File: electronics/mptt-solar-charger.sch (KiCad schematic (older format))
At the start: 46 parts

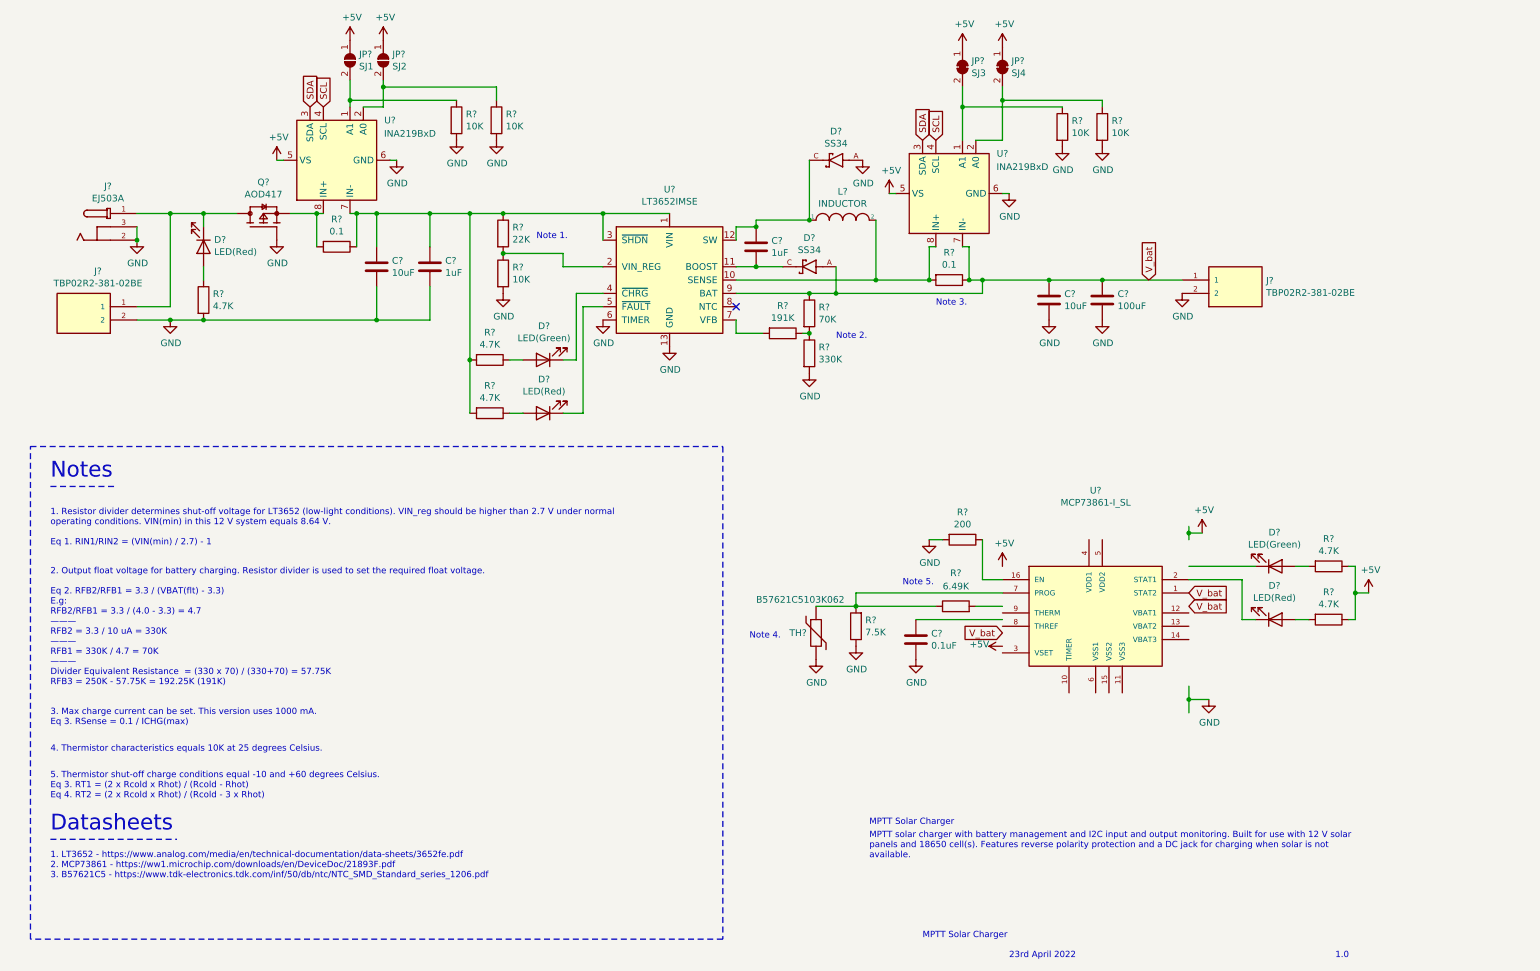
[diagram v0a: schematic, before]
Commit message: updated mcp73861 symbol
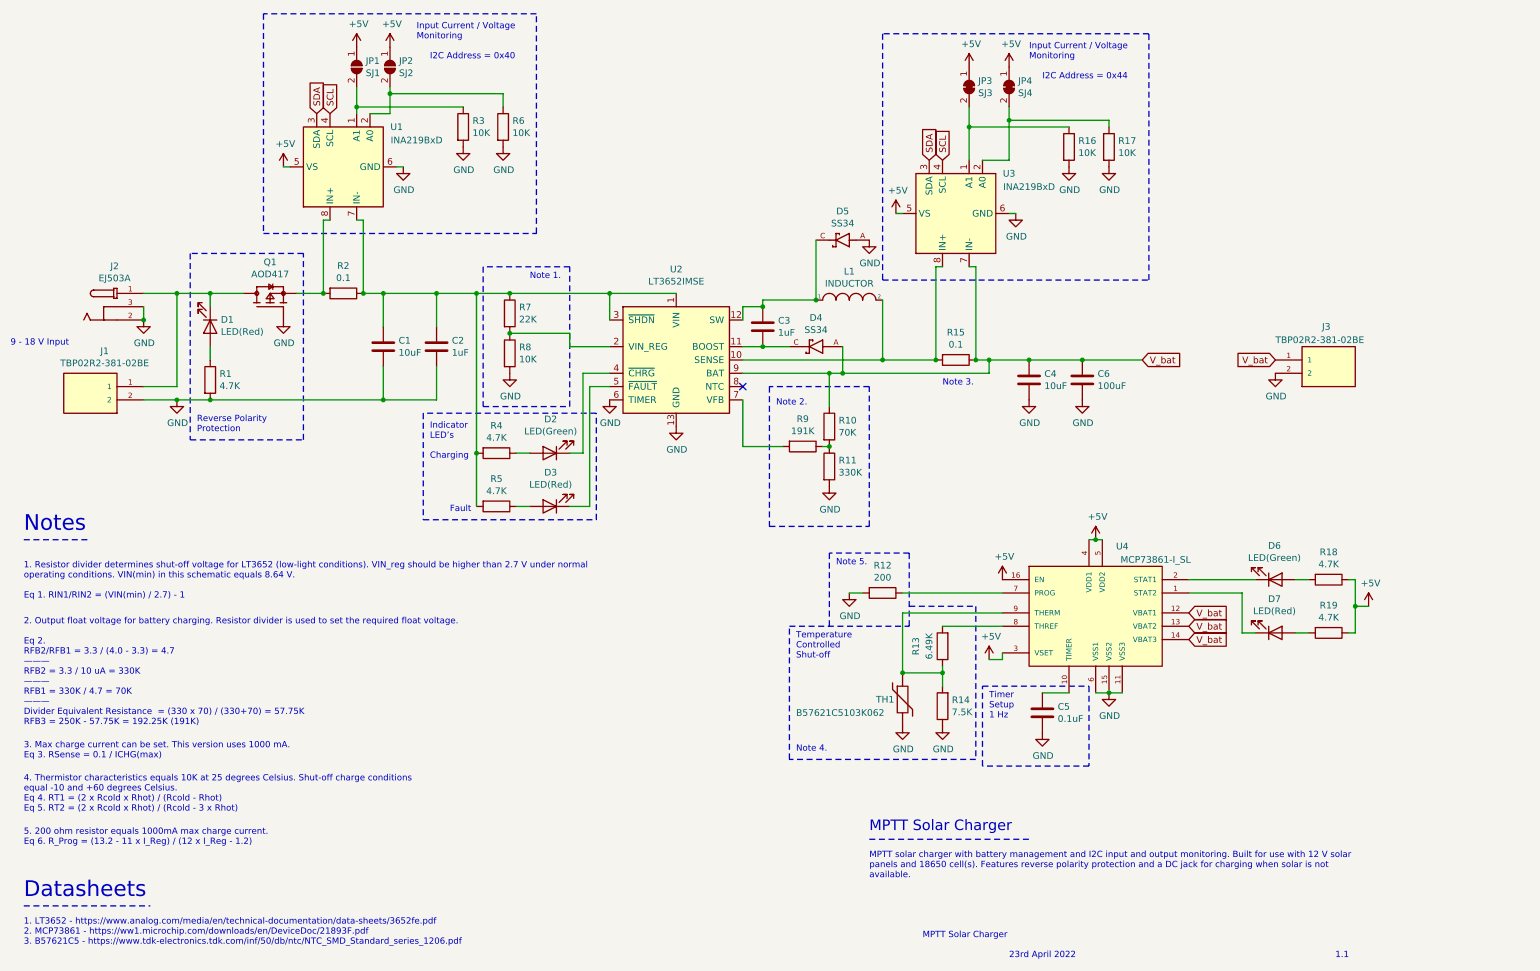
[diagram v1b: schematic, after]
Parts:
- gave numbers to parts that had none: 46
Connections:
- wire segments 113 -> 114
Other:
- note added: "1. Resistor divider determines shut-off voltage for LT3652 (low-light conditions). VIN_reg should be higher than 2.7 V under normal \noperating conditions. VIN(min) in this schematic equals 8.64 V.\n\nEq 1. RIN1/RIN2 = (VIN(min) / 2.7) - 1"
- note added: "1.1"
- note added: "2. Output float voltage for battery charging. Resistor divider is used to set the required float voltage. \n\nEq 2. \nRFB2/RFB1 = 3.3 / (4.0 - 3.3) = 4.7\n———\nRFB2 = 3.3 / 10 uA = 330K\n———\nRFB1 = 330K / 4.7 = 70K\n———\nDivider Equivalent Resistance = (330 x 70) / (330+70) = 57.75K\nRFB3 = 250K - 57.75K = 192.25K (191K)"
- note added: "4. Thermistor characteristics equals 10K at 25 degrees Celsius. Shut-off charge conditions \nequal -10 and +60 degrees Celsius. \nEq 4. RT1 = (2 x Rcold x Rhot) / (Rcold - Rhot)\nEq 5. RT2 = (2 x Rcold x Rhot) / (Rcold - 3 x Rhot)"
- note added: "5. 200 ohm resistor equals 1000mA max charge current.\nEq 6. R_Prog = (13.2 - 11 x I_Reg) / (12 x I_Reg - 1.2)"
- note added: "9 - 18 V Input"
- note added: "Charging"
- note added: "Fault"
- note added: "I2C Address = 0x40"
- note added: "I2C Address = 0x44"
- note added: "Indicator\nLED’s"
- note added: "Input Current / Voltage\nMonitoring"
- note added: "Reverse Polarity \nProtection"
- note added: "Temperature \nControlled \nShut-off"
- note added: "Timer\nSetup\n1 Hz"
- note removed: "1. Resistor divider determines shut-off voltage for LT3652 (low-light conditions). VIN_reg should be higher than 2.7 V under normal \noperating conditions. VIN(min) in this 12 V system equals 8.64 V.\n\nEq 1. RIN1/RIN2 = (VIN(min) / 2.7) - 1"
- note removed: "1.0"
- note removed: "2. Output float voltage for battery charging. Resistor divider is used to set the required float voltage. \n\nEq 2. RFB2/RFB1 = 3.3 / (VBAT(flt) - 3.3)\nE.g: \nRFB2/RFB1 = 3.3 / (4.0 - 3.3) = 4.7\n———\nRFB2 = 3.3 / 10 uA = 330K\n———\nRFB1 = 330K / 4.7 = 70K\n———\nDivider Equivalent Resistance = (330 x 70) / (330+70) = 57.75K\nRFB3 = 250K - 57.75K = 192.25K (191K)"
- note removed: "4. Thermistor characteristics equals 10K at 25 degrees Celsius."
- note removed: "5. Thermistor shut-off charge conditions equal -10 and +60 degrees Celsius. \nEq 3. RT1 = (2 x Rcold x Rhot) / (Rcold - Rhot)\nEq 4. RT2 = (2 x Rcold x Rhot) / (Rcold - 3 x Rhot)"
- moved on the sheet: C1, C2, C3, C4, C5, C6, D1, D2, D3, D4, D5, D6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

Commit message: removed unneeded bypass cap on LT3652 input
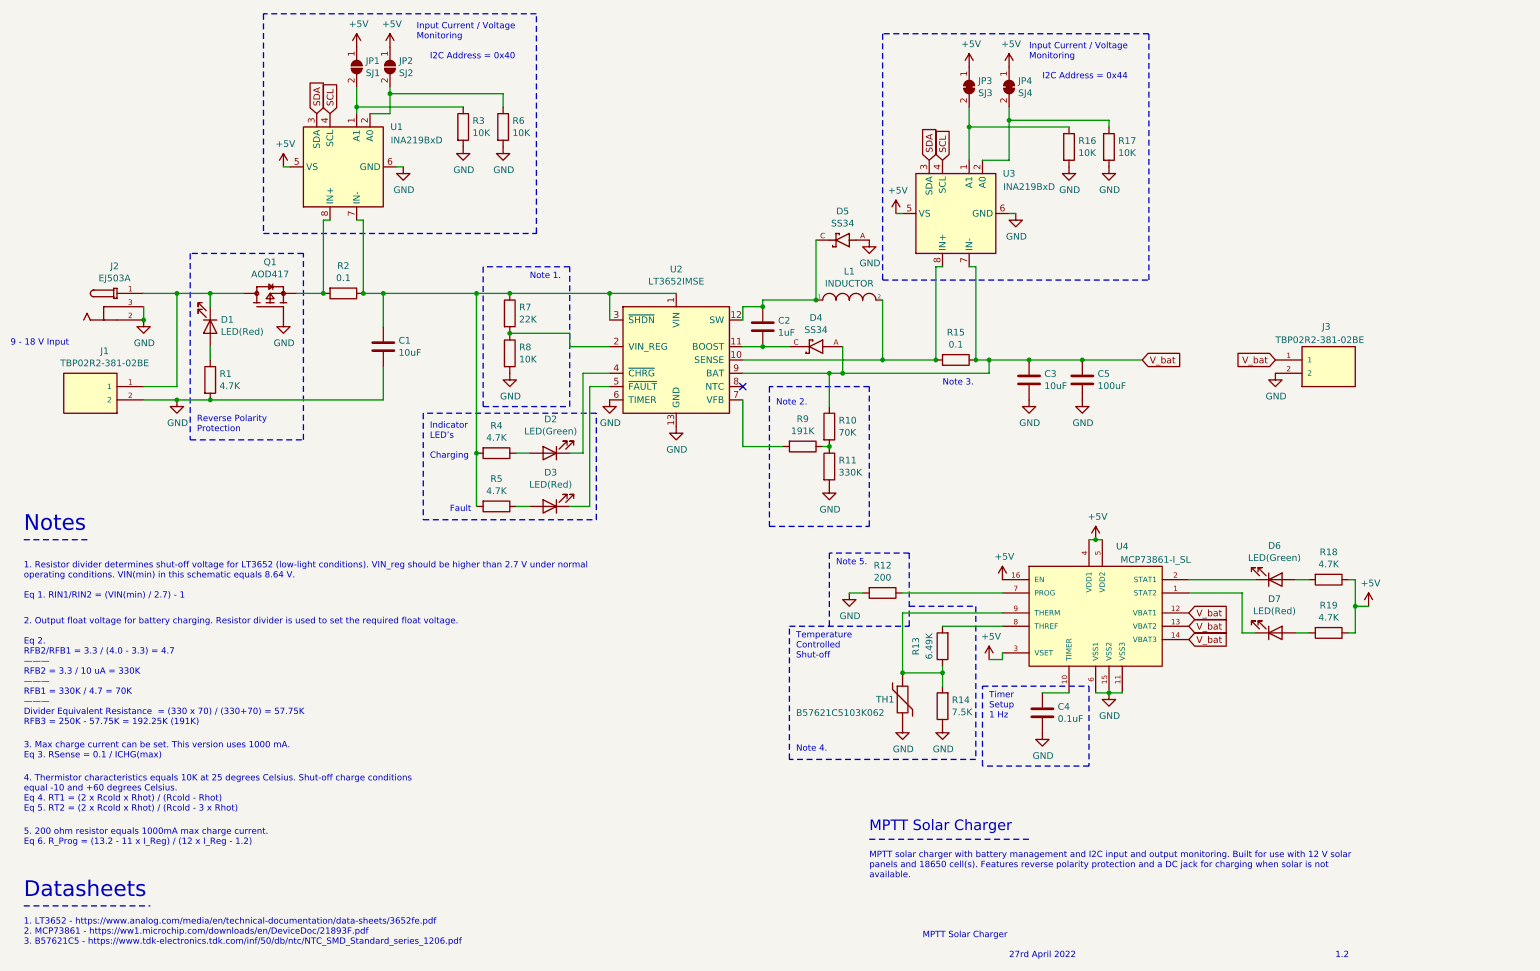
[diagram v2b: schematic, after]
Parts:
- removed C2: 1uF, symbol Device:C
- renumbered C3 to C2, C4 to C3, C5 to C4, C6 to C5
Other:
- note added: "1.2"
- note added: "27rd April 2022"
- note removed: "1.1"
- note removed: "23rd April 2022"
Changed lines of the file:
@@
 	3400 2650 3400 2900
 Connection ~ 2100 3450
-$Comp
-L Device:C C2
-U 1 1 6264ABCC
-P 3800 3050
-F 0 "C2" H 3915 3096 50  0000 L CNN
-F 1 "1uF" H 3915 3005 50  0000 L CNN
-F 2 "" H 3838 2900 50  0001 C CNN
-F 3 "~" H 3800 3050 50  0001 C CNN
-	1    3800 3050
-	1    0    0    -1
-$EndComp
-Wire Wire Line
-	3800 3450 3800 3200
-Wire Wire Line
-	3800 2900 3800 2650
-Wire Wire Line
-	3400 2650 3800 2650
 Wire Wire Line
 	2750 2650 2950 2650
-Connection ~ 3400 3450
 Wire Wire Line
 	2100 3450 3400 3450
@@
 	1    0    0    -1
 $EndComp
-Connection ~ 3800 2650
 Wire Wire Line
 	3400 2650 3250 2650
@@
 	1    0    0    -1
 $EndComp
-Wire Wire Line
-	3400 3450 3800 3450
 $Comp
 L Device:LED D2
@@
 $EndComp
 $Comp
-L Device:C C3
+L Device:C C2
 U 1 1 62671672
 P 6250 2900
-F 0 "C3" H 6365 2946 50  0000 L CNN
+F 0 "C2" H 6365 2946 50  0000 L CNN
 F 1 "1uF" H 6365 2855 50  0000 L CNN
 F 2 "" H 6288 2750 50  0001 C CNN
@@
 Connection ~ 7150 3150
 $Comp
-L Device:C C4
+L Device:C C3
 U 1 1 6267C219
 P 8250 3300
-F 0 "C4" H 8365 3346 50  0000 L CNN
+F 0 "C3" H 8365 3346 50  0000 L CNN
 F 1 "10uF" H 8365 3255 50  0000 L CNN
 F 2 "" H 8288 3150 50  0001 C CNN
@@
 $EndComp
 $Comp
-L Device:C C6
+L Device:C C5
 U 1 1 6267CD75
 P 8650 3300
-F 0 "C6" H 8765 3346 50  0000 L CNN
+F 0 "C5" H 8765 3346 50  0000 L CNN
 F 1 "100uF" H 8765 3255 50  0000 L CNN
 F 2 "" H 8688 3150 50  0001 C CNN
@@
 $EndComp
 $Comp
-L Device:C C5
+L Device:C C4
 U 1 1 626B28CC
 P 8350 5800
-F 0 "C5" H 8465 5846 50  0000 L CNN
+F 0 "C4" H 8465 5846 50  0000 L CNN
 F 1 "0.1uF" H 8465 5755 50  0000 L CNN
 F 2 "" H 8388 5650 50  0001 C CNN
@@
 MPTT solar charger with battery management and I2C input and output monitoring. Built for use with 12 V solar \npanels and 18650 cell(s). Features reverse polarity protection and a DC jack for charging when solar is not \navailable.
 Text Notes 8100 7650 0    47   ~ 0
-23rd April 2022
+27rd April 2022
 Text Notes 10550 7650 0    47   ~ 0
-1.1
+1.2
 Wire Wire Line
 	2950 2650 2950 2100
@@
 Wire Notes Line
 	4800 2450 4150 2450
-Wire Wire Line
-	3800 2650 4100 2650
 Wire Wire Line
 	4900 3250 4900 3850
@@
 Wire Notes Line
 	7050 6750 8250 6750
+Wire Wire Line
+	3400 2650 4100 2650
 $EndSCHEMATC
